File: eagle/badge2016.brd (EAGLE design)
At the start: 135 x 100.5 mm, 121 parts, among them IC1 25AA080SN, IC2 FT231XQ, J1 USB-MICRO, Q2 BC857ALT1SMD, Q2_24MHZ NX5032G, X1 PASSER-07, X10 PAD-1.27X1.27, X11 PAD-1.27X1.27, X12 PAD-1.27X1.27, X13 PAD-1.27X1.27, X14 PAD-1.27X1.27, X15 PAD-1.27X1.27, X16 PAD-1.27X1.27, X17 PAD-1.27X1.27, X18 PAD-1.27X1.27, X19 PAD-1.27X1.27, X2 PASSER-07, X20 PAD-1.27X1.27, X21 PAD-0.5, X3 PASSER-07, X4 PAD-0.5, X5 PAD-0.5, X6 PAD-0.5, X7 PAD-0.5, X8 PAD-1.27X1.27, X9 PAD-1.27X1.27

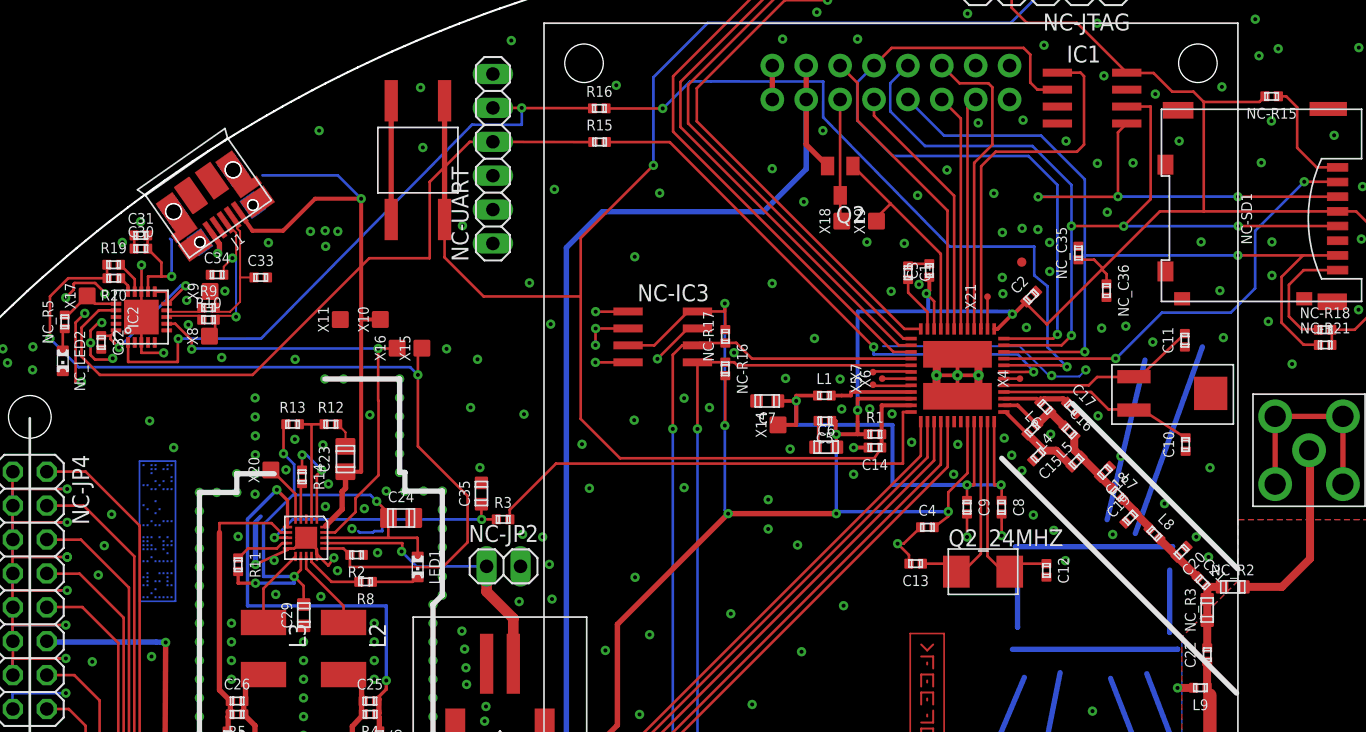
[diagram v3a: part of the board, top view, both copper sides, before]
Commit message: fixed serial lines optimized ground layer below cc1310 changed ltc footprint, less cream fixed missing v_usb line below usb socket
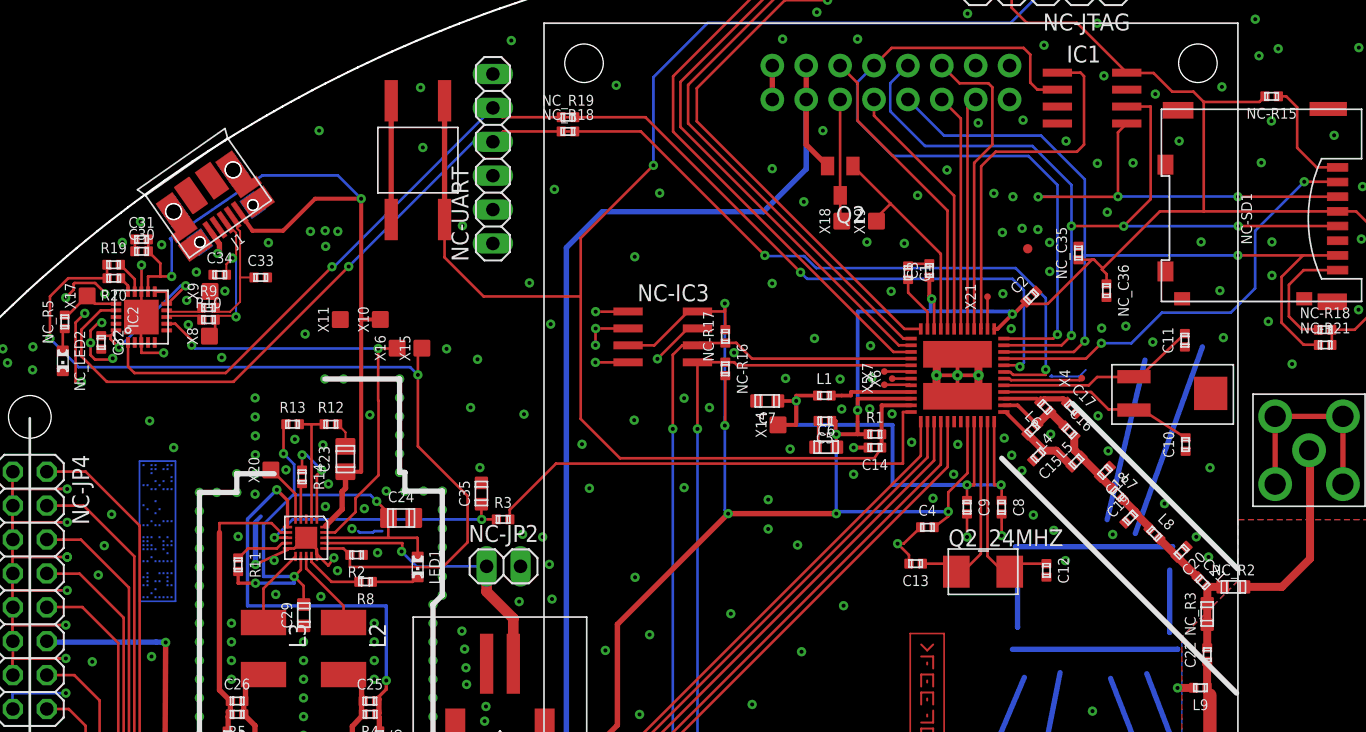
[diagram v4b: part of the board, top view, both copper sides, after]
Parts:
- removed R15, R16: 0, we-rcl:C0402
- added NC_R18, NC_R19: 0, we-rcl:C0402
- moved X4 4.64 mm to (90.8, 62.9)
- moved X3 1.10 mm to (86.8, 72.6)
- moved X7 0.85 mm to (76.0, 63.4)
- moved X5 0.85 mm to (76.0, 62.4)
- moved X6 0.75 mm to (76.6, 62.9)
- moved C31 0.30 mm to (20.3, 73.3)
- moved NC_R3 0.30 mm to (100.2, 45.2)
- moved C30 0.21 mm to (20.3, 72.4)
- moved C34 0.20 mm to (26.2, 70.7)
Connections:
- removed net RXD: IC2.1, NC-UART.5, R16.2
- removed net TXD: IC2.17, NC-UART.4, R15.2
- removed net UART_RXD: R15.1, U$1.7
- removed net UART_TXD: R16.1, U$1.8
- new net FTDI_RXD: IC2.1, NC-UART.5, NC_R19.1, NC_R19.2, U$1.8
- new net FTDI_TXD: IC2.17, NC-UART.4, NC_R18.1, NC_R18.2, U$1.7
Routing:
- net FTDI_TXD: track 0.00 -> 100.2 mm, vias 0 -> 3
- net FTDI_RXD: track 0.00 -> 90.1 mm, vias 0 -> 3
- net TXD: track 54.8 -> 0.00 mm
- net UART_TXD: track 54.4 -> 0.00 mm, vias 2 -> 0
- net RXD: track 48.2 -> 0.00 mm, vias 2 -> 0
- net UART_RXD: track 41.7 -> 0.00 mm, vias 2 -> 0
- net GND: track 224.3 -> 209.3 mm, vias 348 -> 350
- net VUSB_IN: track 56.4 -> 64.4 mm
- net N$14: track 1.20 -> 5.95 mm
- net 3V3: track 285.7 -> 283.3 mm
- net N$38: track 2.92 -> 2.05 mm
- net N$35: track 2.90 -> 2.05 mm
- net N$36: track 2.17 -> 1.42 mm

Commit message: fixes ski
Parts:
- added C36: 100µF, we-rcl:C1206
- added R15: 0R3, we-rcl:C0402
- moved C35 3.00 mm to (48.8, 54.3)
- moved R3 3.00 mm to (50.4, 52.3)
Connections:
- new net N$54: C36.2, R15.1
- net GND: now also R15.2
- net N$20: now also C36.1
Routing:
- net SWITCH_DISP: track 36.1 -> 32.3 mm
- net N$20: track 21.4 -> 25.2 mm
- net SWITCH_DISP_2: track 19.3 -> 22.3 mm
- net N$54: track 0.00 -> 1.80 mm
- net GND: vias 350 -> 362
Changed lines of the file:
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@@
 <element name="X19" library="we-rcl" package="PAD-1.27X1.27" value="PAD-1.27X1.27" x="75.415" y="74.67"/>
 <element name="X20" library="we-rcl" package="PAD-1.27X1.27" value="PAD-1.27X1.27" x="30.035" y="56.02"/>
-<element name="R3" library="we-rcl" package="C0402" value="100k" x="47.435" y="52.32" rot="R270"/>
-<element name="C35" library="we-rcl" package="C0603" value="2.2µF" x="45.81" y="54.255"/>
+<element name="R3" library="we-rcl" package="C0402" value="100k" x="50.435" y="52.32" rot="R270"/>
+<element name="C35" library="we-rcl" package="C0603" value="2.2µF" x="48.81" y="54.255"/>
 <element name="X21" library="we-rcl" package="PAD-0.5" value="PAD-0.5" x="83.735" y="69.005"/>
 <element name="NC_R18" library="we-rcl" package="C0402" value="0" x="52.295" y="81.39" rot="R270"/>
 <element name="NC_R19" library="we-rcl" package="C0402" value="0" x="52.3" y="82.455" rot="R270"/>
+<element name="C36" library="we-rcl" package="C1206" value="100µF" x="46.25" y="53.9" rot="R180"/>
+<element name="R15" library="we-rcl" package="C0402" value="0R3" x="46.25" y="57.6" rot="R180"/>
 </elements>
 <signals>
@@
 <wire x1="32.18" y1="50.94" x2="31.98" y2="50.94" width="0.2" layer="1"/>
 <wire x1="31.98" y1="50.94" x2="31.98" y2="51.64" width="0.2" layer="1"/>
-<via x="73.7" y="55.7" extent="1-16" drill="0.3"/>
+<via x="73.7" y="56.25" extent="1-16" drill="0.3"/>
 <via x="68.945" y="57.59" extent="1-16" drill="0.3"/>
 <via x="81.2" y="55.7" extent="1-16" drill="0.3"/>
@@
 <via x="67.3" y="51.6" extent="1-16" drill="0.3"/>
 <via x="67.3" y="53.8" extent="1-16" drill="0.3"/>
-<via x="45.7" y="56.2" extent="1-16" drill="0.3"/>
+<via x="48.2" y="57.2" extent="1-16" drill="0.3"/>
 <via x="49" y="60.2" extent="1-16" drill="0.3"/>
 <via x="57.66" y="37.7" extent="1-16" drill="0.3"/>
@@
 <via x="51" y="66.95" extent="1-16" drill="0.3"/>
 <via x="53.35" y="57.95" extent="1-16" drill="0.3"/>
-<via x="53.9" y="54.65" extent="1-16" drill="0.3"/>
-<via x="61" y="54.7" extent="1-16" drill="0.3"/>
+<via x="55.4" y="52.7" extent="1-16" drill="0.3"/>
+<via x="61.05" y="56.1" extent="1-16" drill="0.3"/>
 <via x="61.1" y="34.2" extent="1-16" drill="0.3"/>
 <via x="66.1" y="38.45" extent="1-16" drill="0.3"/>
@@
 <via x="51.28" y="77.05" extent="1-16" drill="0.3"/>
 <via x="105.05" y="73.11" extent="1-16" drill="0.3"/>
-<via x="99.74" y="73.11" extent="1-16" drill="0.3"/>
+<via x="95.99" y="73.11" extent="1-16" drill="0.3"/>
 <via x="92.71" y="75.34" extent="1-16" drill="0.3"/>
 <via x="82.24" y="90.22" extent="1-16" drill="0.3"/>
@@
 <wire x1="20.33" y1="65.58" x2="20.3" y2="65.61" width="0.2" layer="1"/>
 <wire x1="20.3" y1="65.61" x2="20.3" y2="67.45" width="0.2" layer="1"/>
+<contactref element="R15" pad="2"/>
+<via x="63.1" y="56.1" extent="1-16" drill="0.3"/>
+<via x="65.45" y="56.1" extent="1-16" drill="0.3"/>
+<via x="100.14" y="74.86" extent="1-16" drill="0.3"/>
+<via x="106.69" y="74.86" extent="1-16" drill="0.3"/>
+<via x="106.69" y="75.96" extent="1-16" drill="0.3"/>
+<via x="100.14" y="73.11" extent="1-16" drill="0.3"/>
+<via x="76.1" y="80.9" extent="1-16" drill="0.3"/>
+<via x="77" y="81.6" extent="1-16" drill="0.3"/>
+<via x="78.1" y="82.35" extent="1-16" drill="0.3"/>
+<via x="55.67" y="18.18" extent="1-16" drill="0.3"/>
+<via x="107.66" y="66.01" extent="1-16" drill="0.3"/>
+<via x="107.81" y="71.56" extent="1-16" drill="0.3"/>
 </signal>
 <signal name="3V3">
@@
 <wire x1="46.2" y1="46.9" x2="48.2" y2="44.9" width="0.8" layer="1"/>
 <wire x1="48.2" y1="44.9" x2="48.2" y2="41.5" width="0.8" layer="1"/>
+<contactref element="C36" pad="1"/>
+<wire x1="46.25" y1="52.5" x2="46.2" y2="52.5" width="0.4064" layer="1"/>
+<wire x1="46.2" y1="52.5" x2="46.2" y2="48.8" width="0.4" layer="1"/>
 </signal>
 <signal name="VUSB_IN">
@@
 <signal name="SWITCH_DISP">
 <contactref element="U$1" pad="36"/>
-<wire x1="78.010934375" y1="60.36615" x2="77.4" y2="60.36615" width="0.2" layer="1"/>
-<wire x1="77.4" y1="60.36615" x2="77.4" y2="56.5" width="0.2" layer="1"/>
-<wire x1="77.4" y1="56.5" x2="51.4" y2="56.5" width="0.2" layer="1"/>
 <contactref element="R3" pad="1"/>
-<wire x1="47.935" y1="52.32" x2="47.935" y2="53.035" width="0.2" layer="1"/>
-<wire x1="47.935" y1="53.035" x2="51.4" y2="56.5" width="0.2" layer="1"/>
+<wire x1="78.010934375" y1="60.36615" x2="77.46615" y2="60.36615" width="0.2" layer="1"/>
+<wire x1="77.46615" y1="60.36615" x2="77.25" y2="60.15" width="0.2" layer="1"/>
+<wire x1="77.25" y1="60.15" x2="77.25" y2="56.9" width="0.2" layer="1"/>
+<wire x1="77.25" y1="56.9" x2="75.7" y2="55.35" width="0.2" layer="1"/>
+<wire x1="75.7" y1="55.35" x2="56.15" y2="55.35" width="0.2" layer="1"/>
+<wire x1="56.15" y1="55.35" x2="53.12" y2="52.32" width="0.2" layer="1"/>
+<wire x1="53.12" y1="52.32" x2="50.935" y2="52.32" width="0.2" layer="1"/>
 </signal>
 <signal name="BG_LIGHT">
@@
 <contactref element="C35" pad="2"/>
 <contactref element="R3" pad="2"/>
-<wire x1="46.935" y1="52.32" x2="45.835" y2="52.32" width="0.2" layer="1"/>
-<via x="45.835" y="52.32" extent="1-16" drill="0.3"/>
-<wire x1="45.835" y1="52.32" x2="31.67" y2="52.32" width="0.2" layer="16"/>
+<wire x1="49.935" y1="52.32" x2="48.835" y2="52.32" width="0.2" layer="1"/>
+<via x="48.835" y="52.32" extent="1-16" drill="0.3"/>
+<wire x1="48.835" y1="52.32" x2="31.67" y2="52.32" width="0.2" layer="16"/>
 <wire x1="31.67" y1="52.32" x2="30.3" y2="50.95" width="0.2" layer="16"/>
 <via x="30.3" y="50.95" extent="1-16" drill="0.3"/>
 <wire x1="30.3" y1="50.95" x2="31.27" y2="50.95" width="0.2" layer="1"/>
 <wire x1="31.27" y1="50.95" x2="31.28" y2="50.94" width="0.2" layer="1"/>
-<wire x1="45.81" y1="53.455" x2="45.81" y2="52.345" width="0.2" layer="1"/>
-<wire x1="45.81" y1="52.345" x2="45.835" y2="52.32" width="0.2" layer="1"/>
+<wire x1="48.81" y1="53.455" x2="48.81" y2="52.345" width="0.2" layer="1"/>
+<wire x1="48.81" y1="52.345" x2="48.835" y2="52.32" width="0.2" layer="1"/>
 </signal>
 <signal name="N$42">
@@
 <wire x1="57.76" y1="81.39" x2="52.795" y2="81.39" width="0.2" layer="1"/>
 </signal>
+<signal name="N$54">
+<contactref element="R15" pad="1"/>
+<contactref element="C36" pad="2"/>
+<wire x1="46.25" y1="57.1" x2="46.25" y2="55.3" width="0.4" layer="1"/>
+</signal>
 </signals>

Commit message: newest pcb state
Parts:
- added NC_BLBD_3V3, NC_BLBD_GND, NC_BLBD_PD, NC_BLBD_PU: (no value), we-rcl:C0402
- added NC_BOOTLOADER_BTN: KSEM31G, ERNW_parts:KSEM31G
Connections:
- removed net N$38: U$1.30, X7.1
- new net BOOTLOADER_BACKDOOR: NC_BLBD_PD.2, NC_BLBD_PU.2, NC_BOOTLOADER_BTN.B1, NC_BOOTLOADER_BTN.B2, U$1.30, X7.1
- new net N$55: NC_BLBD_3V3.2, NC_BLBD_GND.2, NC_BOOTLOADER_BTN.A1, NC_BOOTLOADER_BTN.A2
- net 3V3: now also NC_BLBD_3V3.1, NC_BLBD_PU.1
- net GND: now also NC_BLBD_GND.1, NC_BLBD_PD.1
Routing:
- net BOOTLOADER_BACKDOOR: track 0.00 -> 49.5 mm, vias 0 -> 2
- net 3V3: track 283.3 -> 319.6 mm, vias 10 -> 11
- net N$55: track 0.00 -> 12.1 mm
- net N$38: track 2.05 -> 0.00 mm
- net GND: vias 362 -> 361
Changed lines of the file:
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@@
 <element name="C36" library="we-rcl" package="C1206" value="100µF" x="46.25" y="53.9" rot="R180"/>
 <element name="R15" library="we-rcl" package="C0402" value="0R3" x="46.25" y="57.6" rot="R180"/>
+<element name="NC_BOOTLOADER_BTN" library="ERNW_parts" package="KSEM31G" value="KSEM31G" x="46.25" y="62.5" rot="R90"/>
+<element name="NC_BLBD_PD" library="we-rcl" package="C0402" value="" x="50.65" y="66.65" rot="R270"/>
+<element name="NC_BLBD_PU" library="we-rcl" package="C0402" value="" x="50.65" y="67.7" rot="R270"/>
+<element name="NC_BLBD_GND" library="we-rcl" package="C0402" value="" x="41.6" y="67.05" rot="R90"/>
+<element name="NC_BLBD_3V3" library="we-rcl" package="C0402" value="" x="41.6" y="68.05" rot="R90"/>
 </elements>
 <signals>
@@
 <via x="14.77" y="49.5" extent="1-16" drill="0.3"/>
 <via x="14.77" y="47" extent="1-16" drill="0.3"/>
-<via x="14.77" y="49.5" extent="1-16" drill="0.3"/>
 <via x="14.67" y="39.3" extent="1-16" drill="0.3"/>
 <via x="14.67" y="41.9" extent="1-16" drill="0.3"/>
@@
 <via x="37.78" y="40.34" extent="1-16" drill="0.3"/>
 <via x="94.1" y="66.8" extent="1-16" drill="0.3"/>
-<via x="72.8" y="29.2" extent="1-16" drill="0.3"/>
 <via x="67.3" y="51.6" extent="1-16" drill="0.3"/>
 <via x="67.3" y="53.8" extent="1-16" drill="0.3"/>
-<via x="48.2" y="57.2" extent="1-16" drill="0.3"/>
-<via x="49" y="60.2" extent="1-16" drill="0.3"/>
+<via x="50.45" y="54.85" extent="1-16" drill="0.3"/>
+<via x="49.2" y="61.4" extent="1-16" drill="0.3"/>
 <via x="57.66" y="37.7" extent="1-16" drill="0.3"/>
 <via x="59.23" y="33.08" extent="1-16" drill="0.3"/>
@@
 <via x="18.9" y="73.075" extent="1-16" drill="0.3"/>
 <via x="20.265" y="74.625" extent="1-16" drill="0.3"/>
-<via x="62.9" y="60.7" extent="1-16" drill="0.3"/>
+<via x="62.9" y="61.2" extent="1-16" drill="0.3"/>
 <via x="45.52" y="64.315" extent="1-16" drill="0.3"/>
-<via x="45" y="60.7" extent="1-16" drill="0.3"/>
+<via x="45.4" y="60.95" extent="1-16" drill="0.3"/>
 <via x="48.64" y="46.16" extent="1-16" drill="0.3"/>
 <via x="46.05" y="37.2" extent="1-16" drill="0.3"/>
@@
 <via x="55.1" y="42.5" extent="1-16" drill="0.3"/>
 <via x="54.9" y="29.8" extent="1-16" drill="0.3"/>
-<via x="51" y="66.95" extent="1-16" drill="0.3"/>
-<via x="53.35" y="57.95" extent="1-16" drill="0.3"/>
+<via x="46.15" y="67.15" extent="1-16" drill="0.3"/>
+<via x="53.3" y="58.8" extent="1-16" drill="0.3"/>
 <via x="55.4" y="52.7" extent="1-16" drill="0.3"/>
 <via x="61.05" y="56.1" extent="1-16" drill="0.3"/>
@@
 <via x="14.66" y="68.93" extent="1-16" drill="0.3"/>
 <via x="16.52" y="65.545" extent="1-16" drill="0.3"/>
-<via x="49.41" y="70.04" extent="1-16" drill="0.3"/>
+<via x="49.26" y="71.09" extent="1-16" drill="0.3"/>
 <via x="41.42" y="80.185" extent="1-16" drill="0.3"/>
 <via x="44.39" y="74.325" extent="1-16" drill="0.3"/>
@@
 <via x="107.66" y="66.01" extent="1-16" drill="0.3"/>
 <via x="107.81" y="71.56" extent="1-16" drill="0.3"/>
+<contactref element="NC_BLBD_PD" pad="1"/>
+<contactref element="NC_BLBD_GND" pad="1"/>
+<via x="44.45" y="55.55" extent="1-16" drill="0.3"/>
 </signal>
 <signal name="3V3">
@@
 <wire x1="64.05" y1="59.35" x2="64.075" y2="59.375" width="0.2" layer="1"/>
 <wire x1="64.075" y1="59.375" x2="64.085" y2="63.095" width="0.2" layer="1"/>
-<wire x1="64.05" y1="59.35" x2="64.05" y2="68.5" width="0.2" layer="16"/>
+<wire x1="64.05" y1="59.35" x2="64.05" y2="60.25" width="0.2" layer="16"/>
 <via x="64.05" y="68.5" extent="1-16" drill="0.3"/>
+<wire x1="64.05" y1="60.25" x2="64.05" y2="68.5" width="0.2" layer="16"/>
 <wire x1="64.05" y1="68.5" x2="64.075" y2="68.475" width="0.2" layer="1"/>
 <wire x1="64.075" y1="68.475" x2="64.09" y2="66.535" width="0.2" layer="1"/>
@@
 <wire x1="79.555" y1="68.84" x2="79.485" y2="68.77" width="0.3" layer="16"/>
 <wire x1="79.485" y1="68.77" x2="79.485" y2="67.915" width="0.3" layer="16"/>
+<contactref element="NC_BLBD_PU" pad="1"/>
+<contactref element="NC_BLBD_3V3" pad="1"/>
+<wire x1="64.05" y1="60.25" x2="56.25" y2="60.25" width="0.2" layer="16"/>
+<wire x1="56.25" y1="60.25" x2="53.55" y2="57.55" width="0.2" layer="16"/>
+<via x="53.55" y="57.55" extent="1-16" drill="0.3"/>
+<wire x1="53.55" y1="57.55" x2="52.2" y2="58.9" width="0.2" layer="1"/>
+<wire x1="52.2" y1="58.9" x2="52.2" y2="67.75" width="0.2" layer="1"/>
+<wire x1="52.2" y1="67.75" x2="52.15" y2="67.7" width="0.2" layer="1"/>
+<wire x1="52.15" y1="67.7" x2="51.15" y2="67.7" width="0.2" layer="1"/>
+<wire x1="41.1" y1="68.05" x2="41.1" y2="69.05" width="0.2" layer="1"/>
+<wire x1="41.1" y1="69.05" x2="51.35" y2="69.05" width="0.2" layer="1"/>
+<wire x1="51.35" y1="69.05" x2="51.35" y2="67.7" width="0.2" layer="1"/>
+<wire x1="51.35" y1="67.7" x2="51.15" y2="67.7" width="0.2" layer="1"/>
 </signal>
 <signal name="N$3">
@@
 <wire x1="85.48" y1="89.525" x2="88.085" y2="92.13" width="0.2" layer="16"/>
 <wire x1="43.05" y1="74.79" x2="43.05" y2="71.95" width="0.2" layer="1"/>
-<wire x1="43.05" y1="71.95" x2="45.975" y2="69.025" width="0.2" layer="1"/>
 <wire x1="75.25" y1="56.9" x2="56.2" y2="56.9" width="0.2" layer="1"/>
 <wire x1="56.2" y1="56.9" x2="53.25" y2="59.85" width="0.2" layer="1"/>
 <wire x1="53.25" y1="73.4" x2="58.7" y2="78.85" width="0.2" layer="1"/>
-<wire x1="53.25" y1="59.85" x2="53.25" y2="69.025" width="0.2" layer="1"/>
-<wire x1="53.25" y1="69.025" x2="53.25" y2="73.4" width="0.2" layer="1"/>
-<wire x1="45.975" y1="69.025" x2="53.25" y2="69.025" width="0.2" layer="1"/>
+<wire x1="53.25" y1="59.85" x2="53.25" y2="70.15" width="0.2" layer="1"/>
+<wire x1="53.25" y1="70.15" x2="53.25" y2="73.4" width="0.2" layer="1"/>
 <wire x1="75.8" y1="60.86615" x2="75.8" y2="58.7" width="0.3" layer="1"/>
+<wire x1="43.05" y1="71.95" x2="44.85" y2="70.15" width="0.2" layer="1"/>
+<wire x1="44.85" y1="70.15" x2="53.25" y2="70.15" width="0.2" layer="1"/>
 </signal>
 <signal name="LED_A">
@@
 <wire x1="78.007084375" y1="62.87" x2="76.595" y2="62.87" width="0.2" layer="1"/>
 </signal>
-<signal name="N$38">
+<signal name="BOOTLOADER_BACKDOOR">
 <contactref element="U$1" pad="30"/>
 <contactref element="X7" pad="1"/>
@@
 <wire x1="78.010934375" y1="63.405" x2="78.005934375" y2="63.4" width="0.2" layer="1"/>
 <wire x1="78.005934375" y1="63.4" x2="76.005" y2="63.4" width="0.2" layer="1"/>
+<contactref element="NC_BOOTLOADER_BTN" pad="B2"/>
+<contactref element="NC_BLBD_PD" pad="2"/>
+<contactref element="NC_BLBD_PU" pad="2"/>
+<contactref element="NC_BOOTLOADER_BTN" pad="B1"/>
+<wire x1="48.25" y1="58.05" x2="48.25" y2="66.95" width="0.2" layer="1"/>
+<wire x1="76.005" y1="63.4" x2="66.15" y2="63.4" width="0.2" layer="1"/>
+<wire x1="66.15" y1="63.4" x2="65.1" y2="62.35" width="0.2" layer="1"/>
+<wire x1="65.1" y1="62.35" x2="65.1" y2="58.3" width="0.2" layer="1"/>
+<wire x1="65.1" y1="58.3" x2="64.55" y2="57.75" width="0.2" layer="1"/>
+<wire x1="48.55" y1="58.35" x2="48.25" y2="58.05" width="0.2" layer="1"/>
+<wire x1="48.25" y1="66.95" x2="49.85" y2="66.95" width="0.2" layer="1"/>
+<wire x1="49.85" y1="66.95" x2="50.15" y2="66.65" width="0.2" layer="1"/>
+<wire x1="50.15" y1="66.65" x2="50.15" y2="67.7" width="0.2" layer="1"/>
+<wire x1="64.55" y1="57.75" x2="57.2" y2="57.75" width="0.2" layer="1"/>
+<via x="57.2" y="57.75" extent="1-16" drill="0.3"/>
+<wire x1="57.2" y1="57.75" x2="55.5" y2="57.75" width="0.2" layer="16"/>
+<wire x1="55.5" y1="57.75" x2="53.9" y2="56.15" width="0.2" layer="16"/>
+<via x="53.9" y="56.15" extent="1-16" drill="0.3"/>
+<wire x1="53.9" y1="56.15" x2="48.25" y2="56.15" width="0.2" layer="1"/>
+<wire x1="48.25" y1="56.15" x2="48.25" y2="58.05" width="0.2" layer="1"/>
 </signal>
 <signal name="N$40">
@@
 <wire x1="46.25" y1="57.1" x2="46.25" y2="55.3" width="0.4" layer="1"/>
 </signal>
+<signal name="N$55">
+<contactref element="NC_BOOTLOADER_BTN" pad="A1"/>
+<contactref element="NC_BLBD_GND" pad="2"/>
+<contactref element="NC_BLBD_3V3" pad="2"/>
+<contactref element="NC_BOOTLOADER_BTN" pad="A2"/>
+<wire x1="44.25" y1="58.05" x2="44.25" y2="66.95" width="0.2" layer="1"/>
+<wire x1="44.25" y1="66.95" x2="42.2" y2="66.95" width="0.2" layer="1"/>
+<wire x1="42.2" y1="66.95" x2="42.1" y2="67.05" width="0.2" layer="1"/>
+<wire x1="42.1" y1="67.05" x2="42.1" y2="68.05" width="0.2" layer="1"/>
+</signal>
 </signals>
